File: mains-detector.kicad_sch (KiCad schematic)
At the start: 51 parts, among them J2 FS1000A, J3 GPIOS, J4 ANT, Q1 IRLML2402, SW1 ONOFF, SW1 RESET, U1 TP4065-4.2V-SOT25-R, U3 NE555D, U3 XC6206P332PR-G

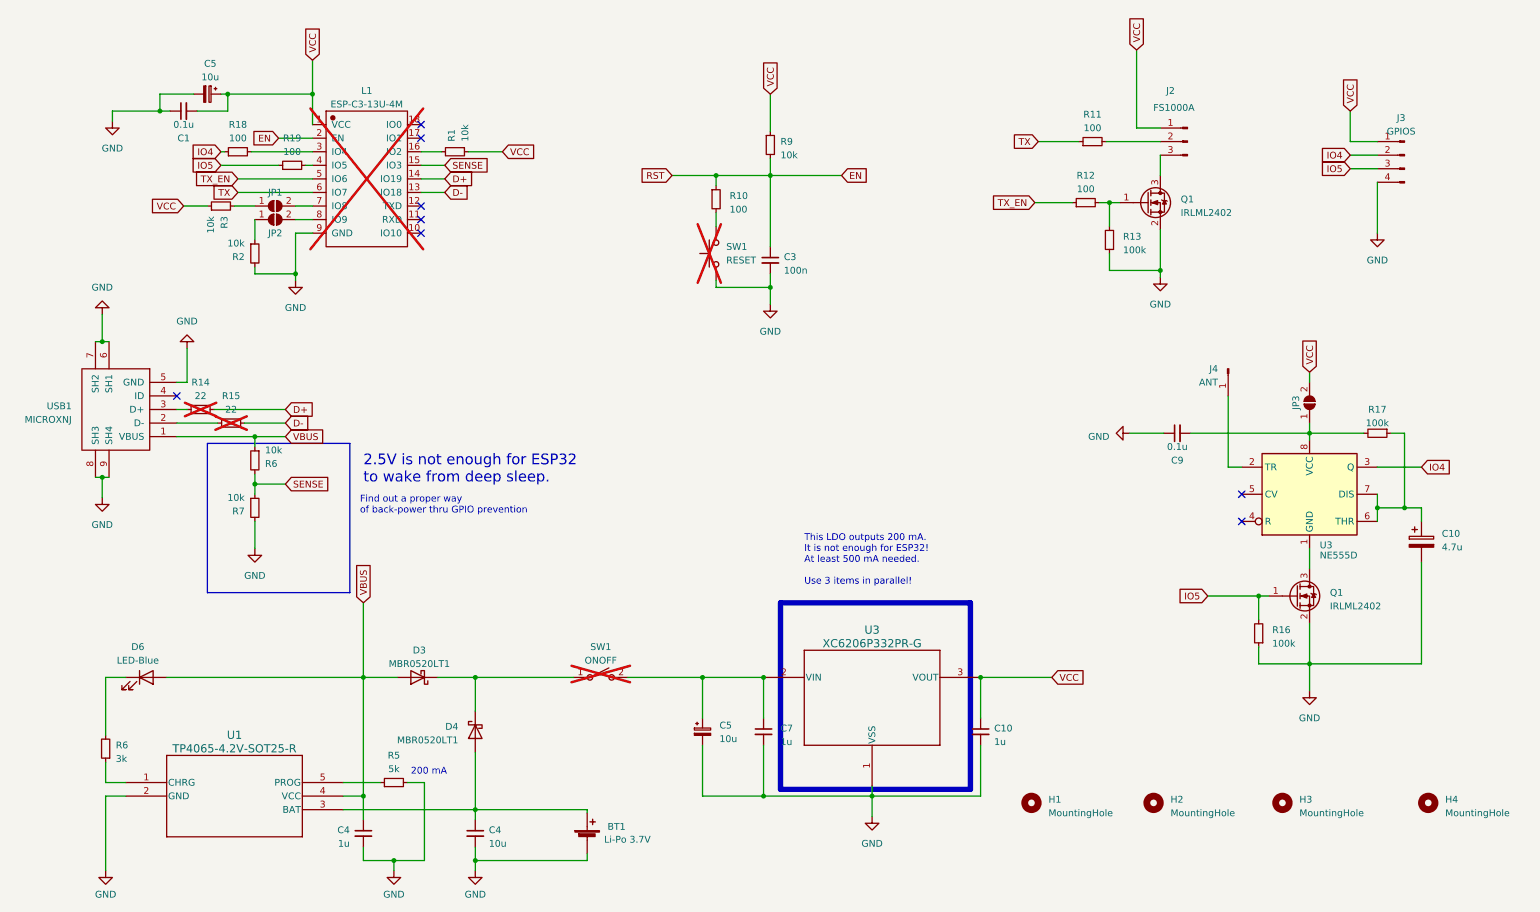
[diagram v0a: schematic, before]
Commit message: Fix schematic / pcb design gaps, update enclosure
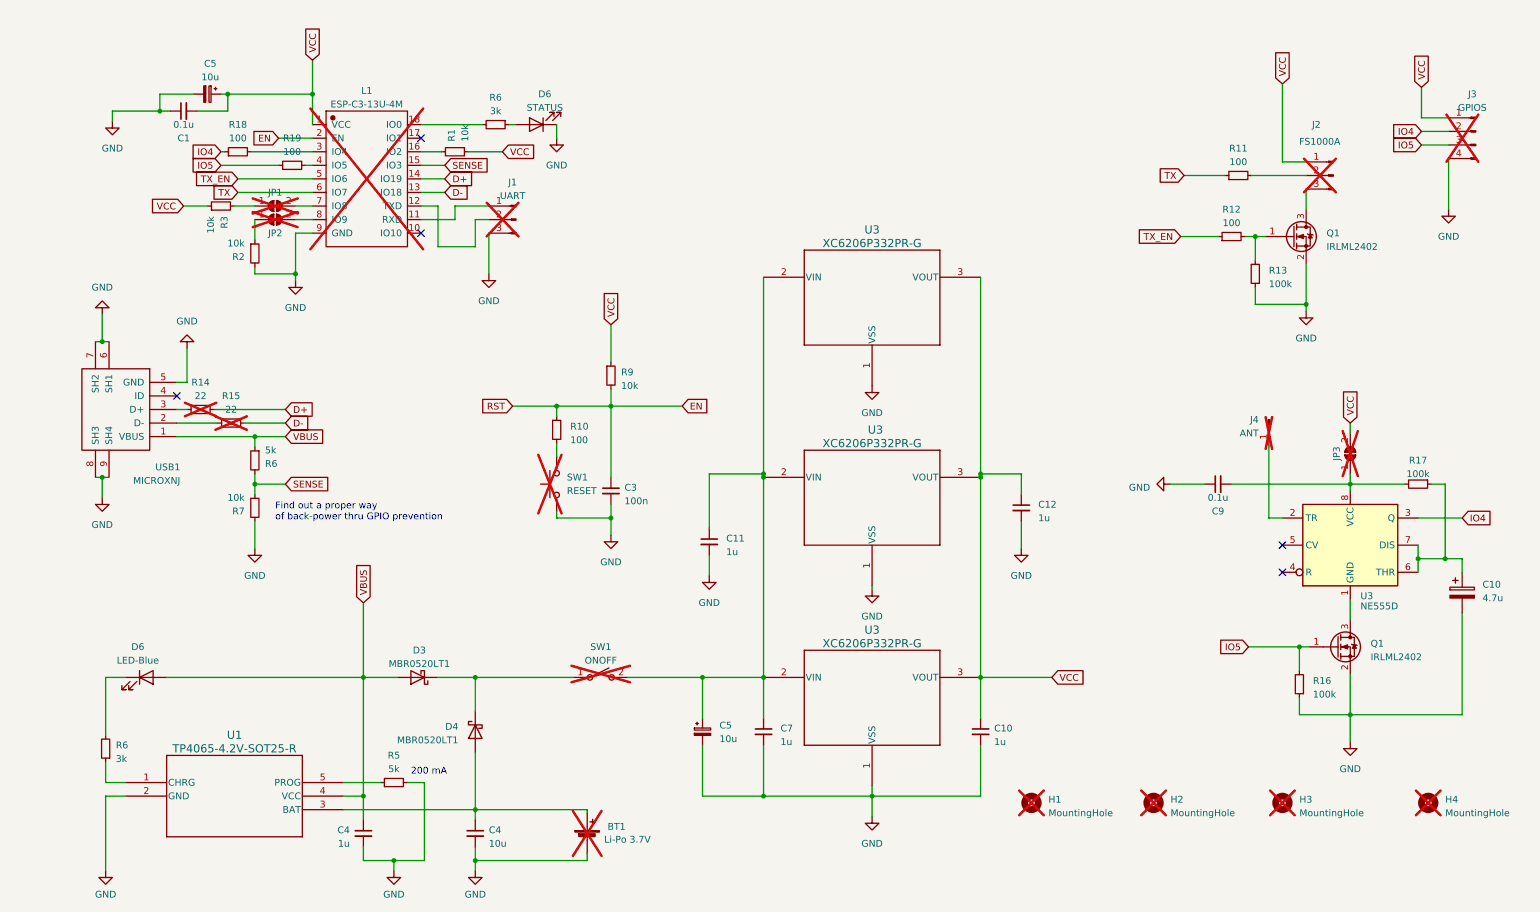
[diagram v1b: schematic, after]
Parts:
- added C11, C12: 1u, Capacitor_SMD:C_0402_1005Metric, symbol Device:C_Small
- added D6: STATUS, LED_SMD:LED_0603_1608Metric, symbol Device:LED
- added J1: UART, Connector_PinHeader_2.54mm:PinHeader_1x03_P2.54mm_Vertical, symbol Connector:Conn_01x03_Pin
- added R6: 3k, Resistor_SMD:R_0402_1005Metric, symbol Device:R_Small
- added U3 (x2): XC6206P332PR-G, footprints:SOT-89_TOR, symbol 2023-10-08_20-10-52:XC6206P332PR-G
- BT1, H1, H2, H3, H4, J2, J3, J4, JP1, JP2, JP3: now not fitted; now left out of the parts list
- C1, C3, C9: LCSC (none) -> C307331
- C10: LCSC (none) -> C2158112
- C10, C7: LCSC (none) -> C52923
- C4: LCSC C15850 -> C96446
- C4: LCSC C15850 -> C52923
- C5: LCSC (none) -> C7171
- D3, D4: LCSC (none) -> C8598
- D6: LCSC C688886 -> C2286
- L1: LCSC (none) -> C2838651
- Q1: LCSC C5364307 -> C20917
- R1, R2, R3, R7, R9: LCSC (none) -> C25744
- R10, R11, R12, R18, R19: LCSC (none) -> C25076
- R13, R16, R17: LCSC (none) -> C25741
- R5: LCSC C17661 -> C25905
- R6: value 10k -> 5k; LCSC (none) -> C25905
- R6: LCSC C17513 -> C25784
- U1: LCSC (none) -> C113540
- U3: LCSC (none) -> C356725
- U3: LCSC (none) -> C526275
- USB1: LCSC (none) -> C404969
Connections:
- net GND: now also C11.2, C12.2, D6.1 (K), J1.3 (Pin_3), U3.1 (VSS), U3.1 (VSS)
- net VCC: now also C12.1, U3.3 (VOUT), U3.3 (VOUT)
- net at L1.11 (RXD): now also J1.1 (Pin_1)
- net at L1.12 (TXD): now also J1.2 (Pin_2)
- net at L1.18 (IO0): now also R6.2
- net at C5.1, C7.1, SW1.2 (B)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: now also C11.1, U3.2 (VIN), U3.2 (VIN)
- new net: D6.2 (A), R6.1
- no-connect marks 8 -> 5
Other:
- note removed: "2.5V is not enough for ESP32 to wake from deep sleep."
- note removed: "This LDO outputs 200 mA. It is not enough for ESP32! At least 500 mA needed. Use 3 items in parallel!"
- moved on the sheet: C10, C3, C9, Q1, R10, R11, R12, R13, R16, R17, R9, SW1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
